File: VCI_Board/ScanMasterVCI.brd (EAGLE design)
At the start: 53 x 39.4 mm, 82 parts, among them IC1 XMEGA16A4A, Q1 MMBT4403, Q10 ZXMP6A17G, Q2 MMBT3904, Q3 MMBT3904, Q4 MMBT3904, Q5 MMBT3904, Q6 MMBT3904, Q7 NTZD5110N, Q8 NTZD5110N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

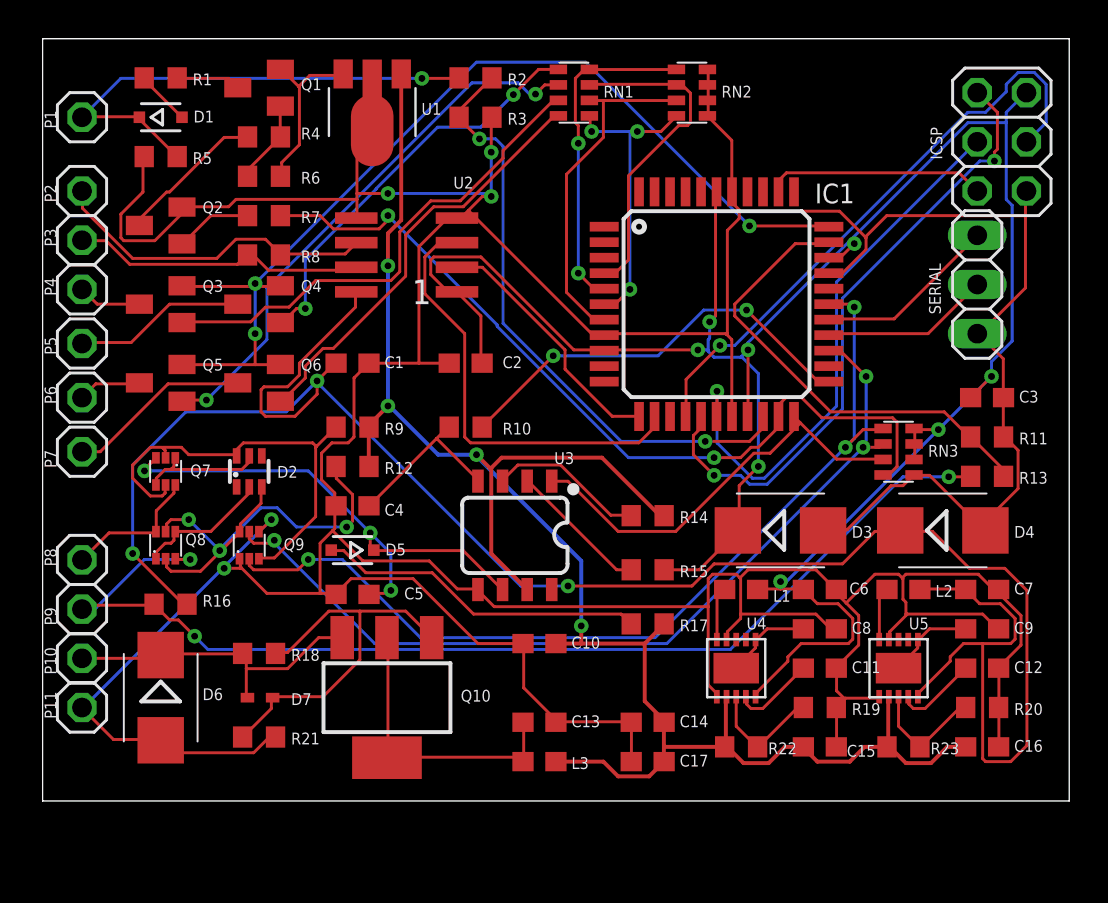
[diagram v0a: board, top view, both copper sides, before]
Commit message: Widened +12V trace, re-named pins
I had ran a part renaming script before and forgot to change the names of the OBD  pins back to what they're supposed to be.
I'm not sure if it's necessary, but I'm making the trace for the +12v rail significantly wider, since it will carry the most current. At this point I'm unsure if I need to do this to the 3.3 and 5v rails.
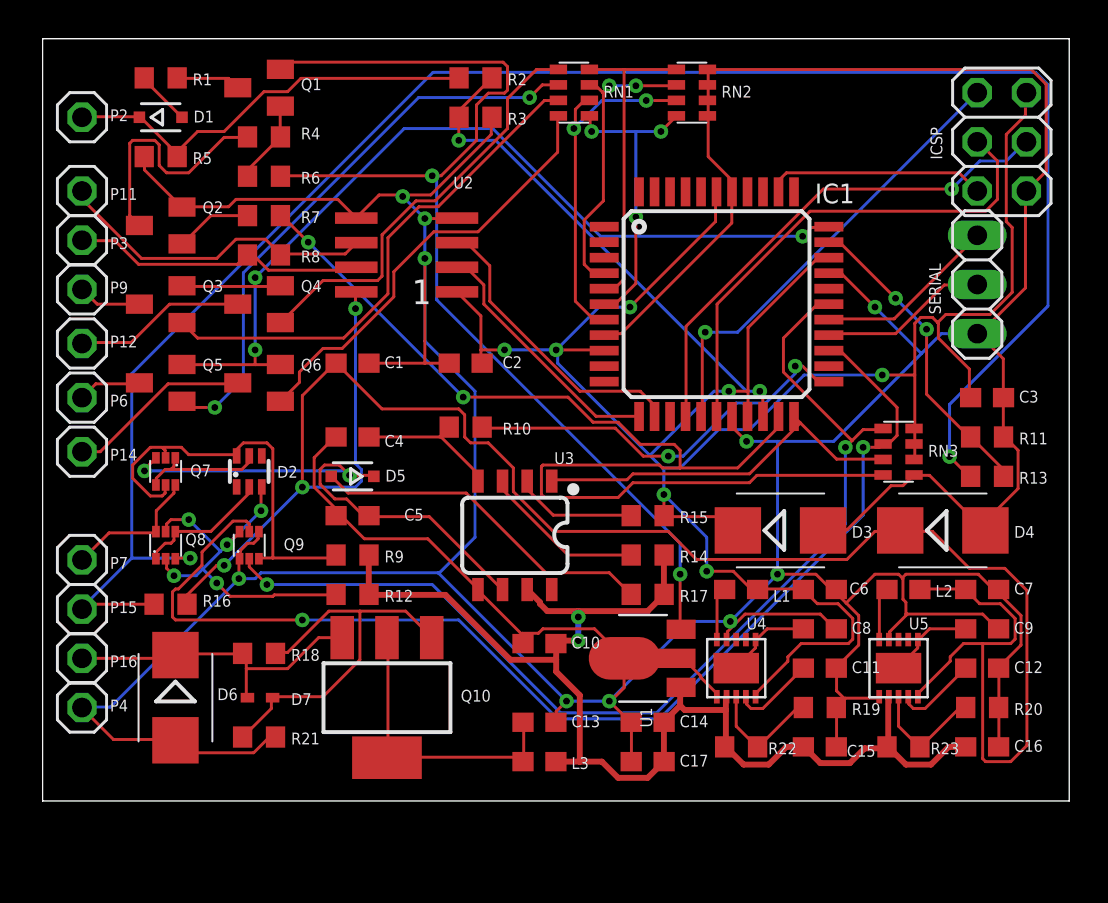
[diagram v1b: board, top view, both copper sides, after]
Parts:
- removed P1, P8: (no value), pinhead:1X01
- added P14, P15: (no value), pinhead:1X01
- moved U1 31.5 mm to (31.0, 9.91), turned to 90 degrees
- moved P11 26.7 mm to (2.03, 34.0)
- moved P4 21.6 mm to (2.03, 7.37)
- moved P9 16.5 mm to (2.03, 29.0)
- moved R12 6.60 mm to (16.0, 13.2)
- moved R9 6.60 mm to (16.0, 15.2)
- moved P7 5.59 mm to (2.03, 15.0)
- moved C5 4.06 mm to (16.0, 17.3)
- moved D5 3.81 mm to (16.0, 19.3)
- moved P2 3.81 mm to (2.03, 37.8)
- moved C4 3.56 mm to (16.0, 21.3)
- moved R15 2.79 mm to (31.2, 17.3)
- moved R14 2.03 mm to (31.2, 15.2)
- moved R17 1.52 mm to (31.2, 13.2)
- moved D6 0.76 mm to (6.86, 7.87)
- renumbered P10 to P16, P5 to P12
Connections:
- net GND: now also P4.1; no longer P11.1
- net J1962-11: now also P11.1; no longer P2.1
- net J1962-14: now also P14.1; no longer P7.1
- net J1962-15: now also P15.1; no longer P9.1
- net J1962-2: now also P2.1; no longer P1.1
- net J1962-7: now also P7.1; no longer P8.1
- net J1962-9: now also P9.1; no longer P4.1
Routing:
- net +8V: track 8.96 -> 56.6 mm, vias 0 -> 2
- net J1962-15: track 58.1 -> 97.7 mm, vias 3 -> 2
- net +12V: track 98.8 -> 65.3 mm, vias 4 -> 2
- net J1850VPW-TX: track 43.5 -> 60.0 mm
- net ISO-K-EN: track 46.0 -> 61.5 mm, vias 3 -> 2
- net GND: track 288.4 -> 303.7 mm, vias 5 -> 10
- net MISO: track 32.6 -> 23.6 mm, vias 2 -> 1
- net SCI-RX: track 24.3 -> 16.2 mm, vias 0 -> 2
- net CCD-TX: track 22.9 -> 15.4 mm
- net SCI-A-TX-EN: track 48.3 -> 54.5 mm, vias 3 -> 2
- net +5V: track 107.6 -> 102.0 mm
- net J1850VPW-RX: track 31.7 -> 26.2 mm
- net N$26: track 7.66 -> 12.7 mm
- net MOSI: track 31.0 -> 26.2 mm
- net J1962-2: track 26.2 -> 22.3 mm, vias 1 -> 0
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
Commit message: Widened more power rails
Widened ground trace to 10 mil, reduced +12v to 10 mil. This should be fine as long as the manufacturer can guarantee 1.5 oz/ft2 copper in traces, it should hold over 1 amp.
+5v and +3.3v also widened slightly, to 8 mil.
Ripped up all traces and re-routed. Seems to still be working, but number of vias is up a bit.
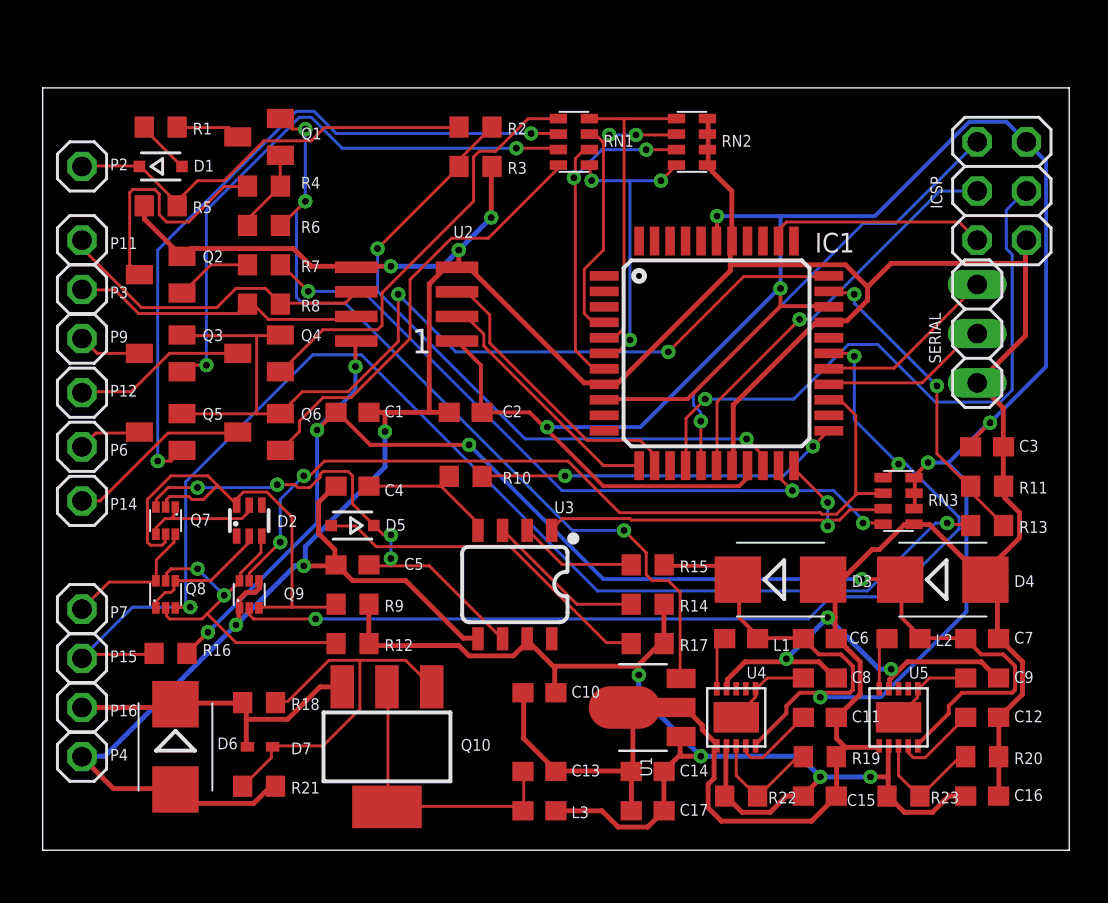
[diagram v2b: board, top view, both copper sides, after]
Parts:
- moved P11 2.54 mm to (2.03, 31.5)
- moved P14 2.54 mm to (2.03, 18.0)
- moved Q2 2.54 mm to (6.10, 29.7)
- moved R10 2.54 mm to (21.8, 19.3)
- moved R8 2.54 mm to (11.4, 28.2)
- moved RN3 2.54 mm to (44.2, 18.0)
- moved U2 2.54 mm to (18.8, 28.2)
- moved D3 2.54 mm to (38.1, 14.0)
- moved D4 2.54 mm to (46.5, 14.0)
- moved P16 2.54 mm to (2.03, 7.37)
- moved P7 2.54 mm to (2.03, 12.4)
- moved R12 2.54 mm to (16.0, 10.7)
- moved R14 2.54 mm to (31.2, 12.7)
- moved R17 2.54 mm to (31.2, 10.7)
- moved R9 2.54 mm to (16.0, 12.7)
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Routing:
- net GND: track 303.7 -> 260.9 mm, vias 10 -> 9
- net +5V: track 102.0 -> 70.6 mm, vias 3 -> 5
- net J1962-15: track 97.7 -> 67.6 mm
- net J1850VPW-TX: track 60.0 -> 38.3 mm, vias 2 -> 3
- net ISO-K-EN: track 61.5 -> 44.2 mm
- net +3V3: track 119.5 -> 136.6 mm, vias 7 -> 6
- net +8V: track 56.6 -> 43.4 mm, vias 2 -> 3
- net J1850VPW-RX: track 26.2 -> 34.9 mm
- net MOSI: track 26.2 -> 33.2 mm
- net N$21: track 29.7 -> 36.5 mm
- net SCK: track 26.0 -> 21.3 mm, vias 0 -> 1
- net N$22: track 26.5 -> 30.3 mm, vias 0 -> 2
- net N$11: track 22.0 -> 25.6 mm
- net ISO-K-RX: track 19.6 -> 21.8 mm, vias 0 -> 2
- net ISO-K-TX: track 21.0 -> 18.9 mm
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
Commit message: Fixed an erroneous pin assignment. The MAX17502 as I specified it had the bottom exposed pad connected to a random pin, when it should be ground. Fixed. Besides that, mostly small changes, prepping for sending it off for production.
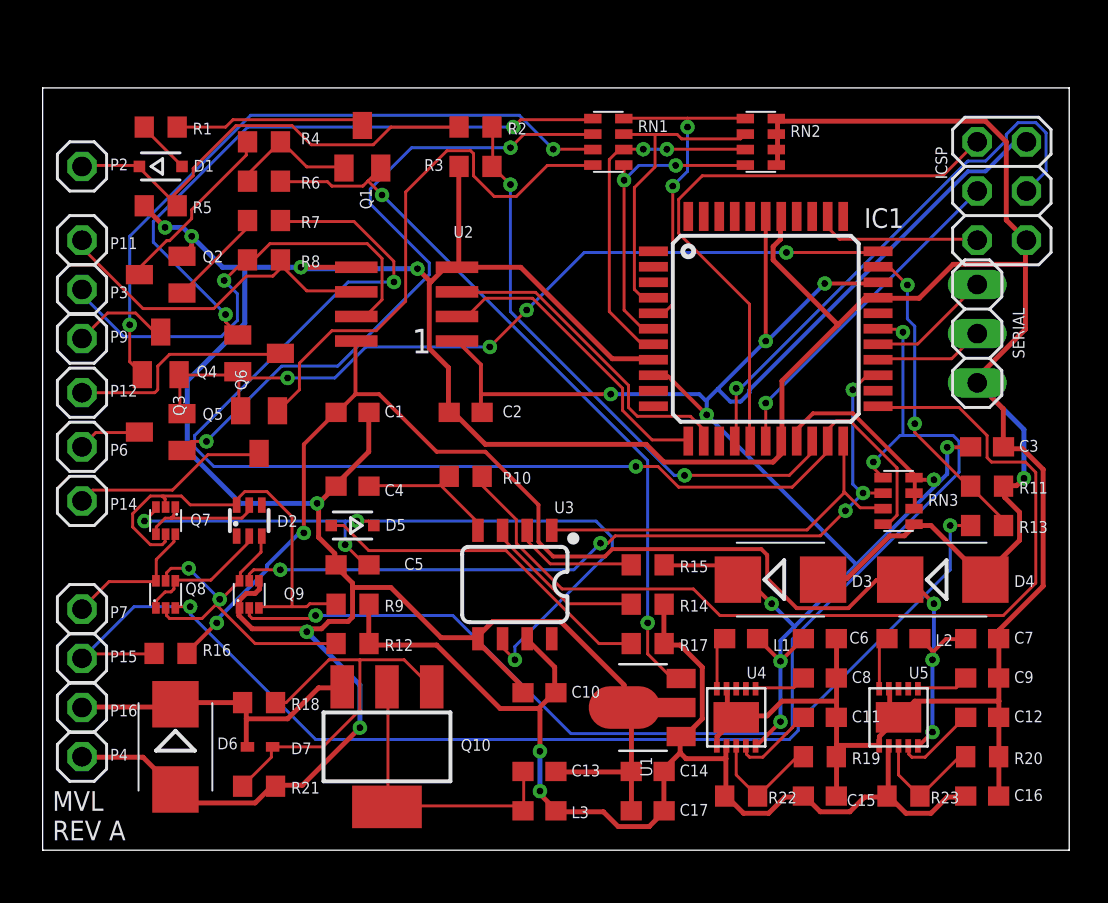
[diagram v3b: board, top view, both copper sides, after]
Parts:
- moved Q1 5.36 mm to (16.5, 36.3), turned to 0 degrees
- moved RN2 3.56 mm to (37.1, 36.6)
- moved IC1 2.84 mm to (37.3, 26.9)
- moved R4 2.29 mm to (11.4, 36.6)
- moved R7 2.29 mm to (11.4, 32.5)
- moved R8 2.29 mm to (11.4, 30.5)
- moved R6 2.29 mm to (11.4, 34.5)
- moved RN1 1.78 mm to (29.2, 36.6)
- turned Q3 to 0 degrees
- turned Q4 to 270 degrees
- turned Q6 to 180 degrees
- turned R3 to 0 degrees
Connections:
- net GND: now also U4.EPAD, U5.EPAD
- net N$17: no longer U5.P$11
- net N$3: no longer U4.P$11
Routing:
- net GND: track 260.9 -> 293.9 mm, vias 9 -> 8
- net ISO-K-TX: track 18.9 -> 49.2 mm, vias 2 -> 0
- net J1850VPW-TX: track 38.3 -> 65.6 mm, vias 3 -> 2
- net +3V3: track 136.6 -> 114.6 mm, vias 6 -> 9
- net ISO-K: track 25.6 -> 39.1 mm
- net N$13: track 22.1 -> 32.6 mm, vias 0 -> 2
- net J1962-3: track 15.3 -> 25.0 mm, vias 0 -> 1
- net SCI-A-TX-EN: track 52.9 -> 62.4 mm
- net MISO: track 23.9 -> 30.7 mm, vias 1 -> 0
- net J1962-15: track 67.6 -> 60.9 mm
- net N$29: track 3.34 -> 9.85 mm
- net SCI-TX: track 49.4 -> 43.4 mm, vias 2 -> 4
- net N$23: track 22.6 -> 28.3 mm
- net +8V: track 43.4 -> 38.3 mm, vias 3 -> 2
- net MOSI: track 33.2 -> 28.3 mm
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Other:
- board text added: "MVL REV A"

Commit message: Made component dimension mods based on prototype PCB. Ordered rev A board, discovered that I hadn't paid close enough attention to part dimensions. In particular the ISO1050 and MAX17502 chips were completely wrong, and the 1.5SMC43AT3G ESD diode was SMC package, not SMB. The ISO1050 fit with modification, and the diode was close enough to solder, but the MAX17502 pins touched the ground pad so the board can't be assembled. Made modifications based on my findings, bumped the revision to B, and am looking at ordering new boards.
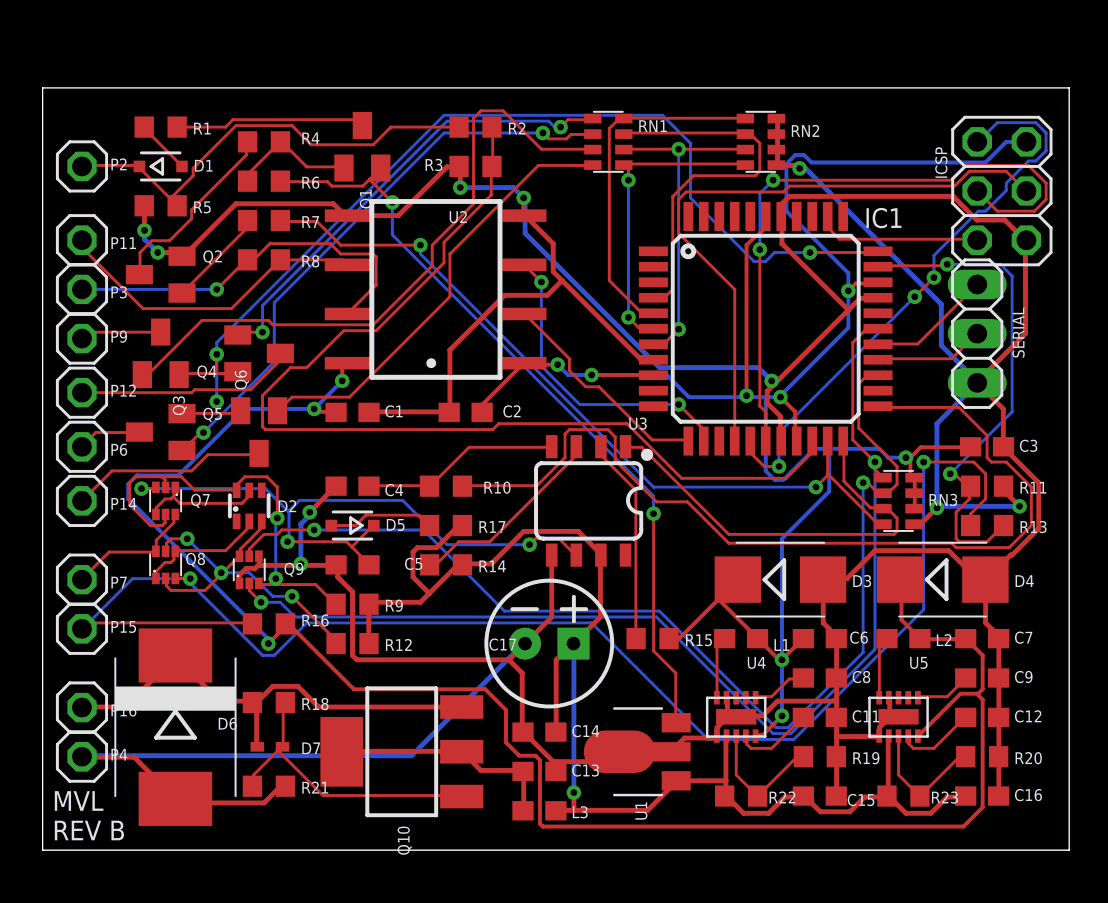
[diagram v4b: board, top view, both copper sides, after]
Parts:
- removed C10: 0.1uF, adafruit:C0603
- C17: device adafruit:C0603 -> SparkFun-Capacitors:CPOL-RADIAL-2.5MM-6.5MM
- D6: device diode:SMB -> diode:SMC
- U4, U5: device customics:TDFN-10 -> customics:TDFN-10-EP
- moved R17 12.1 mm to (20.8, 16.8)
- moved R14 10.6 mm to (20.8, 14.7)
- moved C17 10.0 mm to (26.2, 10.7), turned to 0 degrees
- moved C14 5.95 mm to (25.7, 6.10)
- moved U3 5.76 mm to (28.2, 18.0)
- moved R16 5.30 mm to (11.7, 11.7)
- moved R15 3.82 mm to (31.5, 10.9)
- moved U1 2.30 mm to (30.7, 5.08)
- moved P7 1.52 mm to (2.03, 14.0)
- moved P15 1.52 mm to (2.03, 11.4)
- moved Q8 1.52 mm to (6.35, 14.7)
- moved Q9 1.27 mm to (10.7, 14.5)
- moved R10 1.14 mm to (20.8, 18.8)
- moved D6 1.02 mm to (6.86, 6.35)
- moved Q7 1.02 mm to (6.35, 18.0)
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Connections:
- net +12V: no longer C10.1
- net GND: no longer C10.2
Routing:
- net J1850VPW-TX: track 65.6 -> 40.2 mm
- net J1850VPW-RX: track 30.1 -> 52.8 mm, vias 2 -> 0
- net +5V: track 68.7 -> 90.9 mm, vias 5 -> 3
- net SCK: track 17.4 -> 33.8 mm, vias 1 -> 2
- net J1962-15: track 60.9 -> 76.1 mm
- net ISO-K-EN: track 42.0 -> 56.5 mm, vias 5 -> 2
- net N$31: track 18.0 -> 5.52 mm
- net SCI-TX: track 43.4 -> 54.9 mm, vias 4 -> 3
- net SCI-RX: track 16.5 -> 26.0 mm
- net GND: track 293.9 -> 285.2 mm, vias 8 -> 10
- net N$13: track 32.6 -> 24.0 mm
- net J1962-16: track 16.5 -> 25.0 mm
- net +12V: track 64.1 -> 70.8 mm, vias 2 -> 1
- net SCI-A-TX-EN: track 62.4 -> 56.4 mm, vias 3 -> 2
- net ISO-K: track 39.1 -> 33.3 mm, vias 4 -> 3
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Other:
- board text added: "MVL REV B"
- board text removed: "MVL REV A"

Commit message: Fixed some trace widths
Some traces that technically carry 12v were sized as non-power traces.  Fixed this.
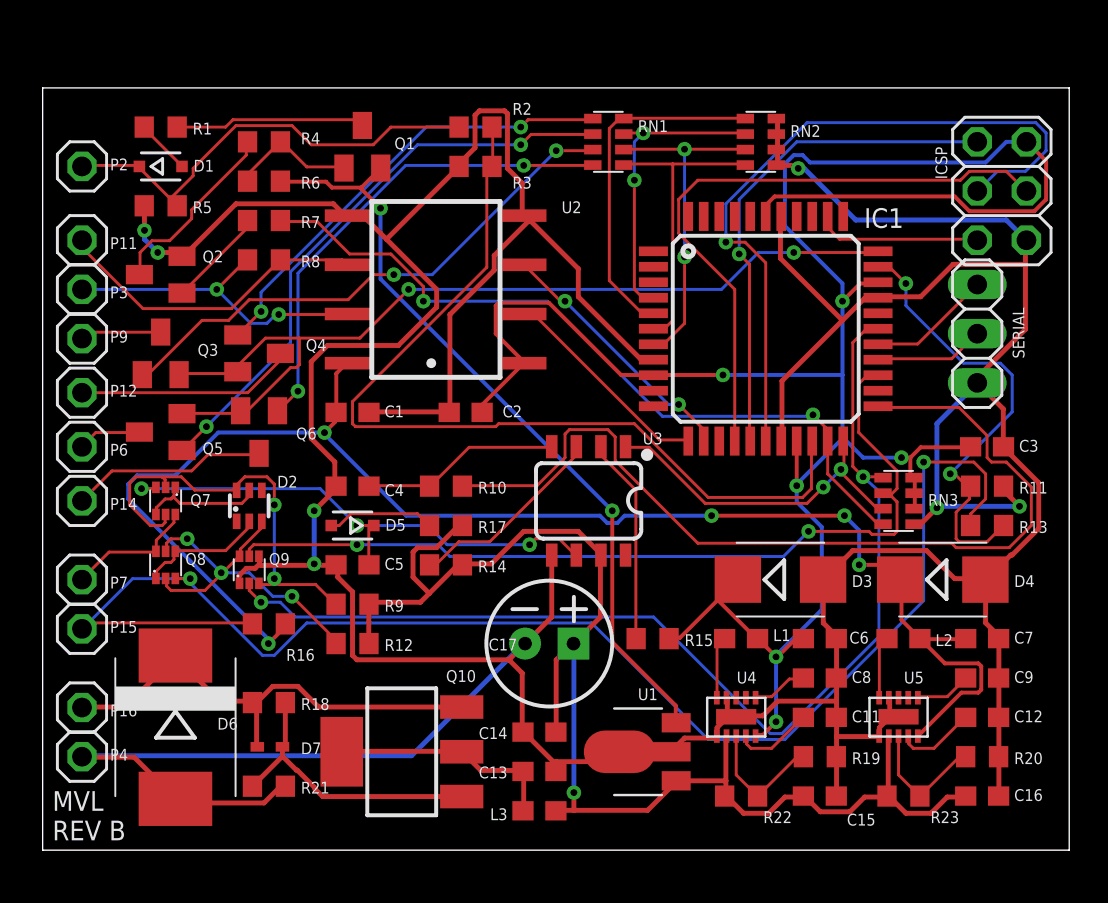
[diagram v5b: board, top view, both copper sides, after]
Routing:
- net +5V: track 90.9 -> 77.4 mm, vias 3 -> 5
- net ISO-K-EN: track 56.5 -> 45.6 mm
- net +3V3: track 110.2 -> 119.8 mm, vias 8 -> 6
- net SCI-TX: track 54.9 -> 47.4 mm, vias 3 -> 2
- net J1850VPW-RX: track 52.8 -> 46.4 mm
- net ISO-K: track 33.3 -> 27.8 mm
- net N$22: track 33.1 -> 28.1 mm, vias 0 -> 2
- net ISO-K-RX: track 22.3 -> 17.8 mm, vias 0 -> 2
- net SCI-A-ENGINE-EN: track 19.8 -> 15.8 mm, vias 0 -> 2
- net SCK: track 33.8 -> 37.5 mm, vias 2 -> 1
- net MISO: track 30.0 -> 26.2 mm, vias 3 -> 1
- net J1962-3: track 20.0 -> 16.9 mm, vias 1 -> 2
- net CCD-TX: track 16.0 -> 13.4 mm
- net SCI-RX: track 26.0 -> 23.6 mm
- net N$23: track 22.8 -> 25.1 mm, vias 0 -> 2
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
